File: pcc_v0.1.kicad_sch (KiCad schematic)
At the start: 54 parts, among them J1 Conn_01x04_Socket, J2 Conn_01x04_Socket, J4 Conn_02x14_Counter_Clockwise, J6 Conn_01x04_Socket, J7 Conn_01x04_Socket, J8 Conn_01x04_Socket, K2 CPC1706, K3 G7L-2A-X-L_DC12, Q2 BS108, U2 4N35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

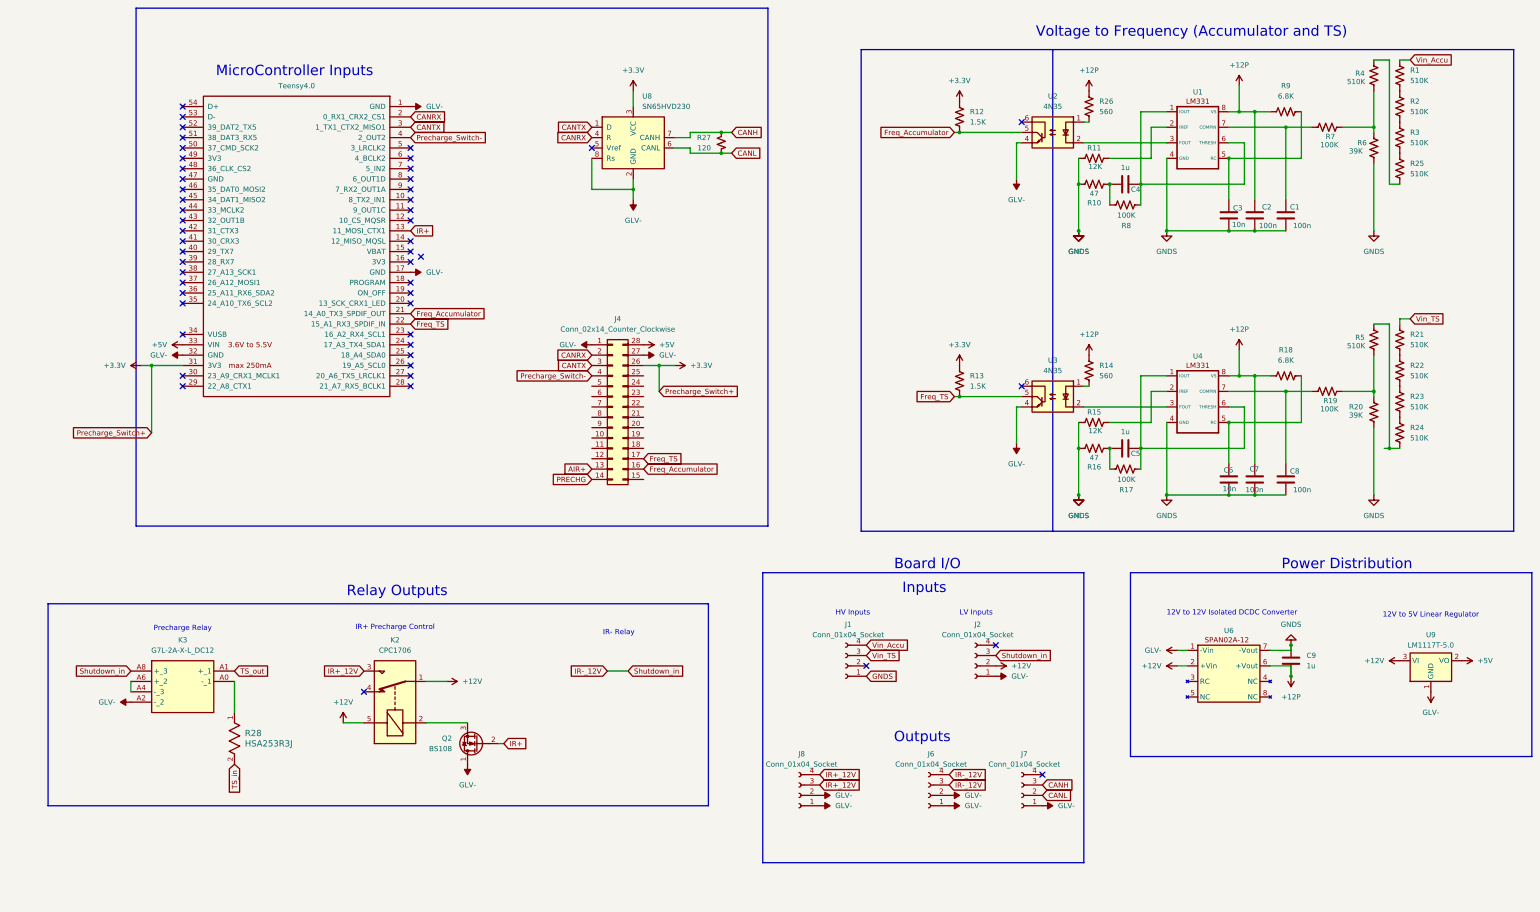
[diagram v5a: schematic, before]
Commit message: looking to add discharge relay
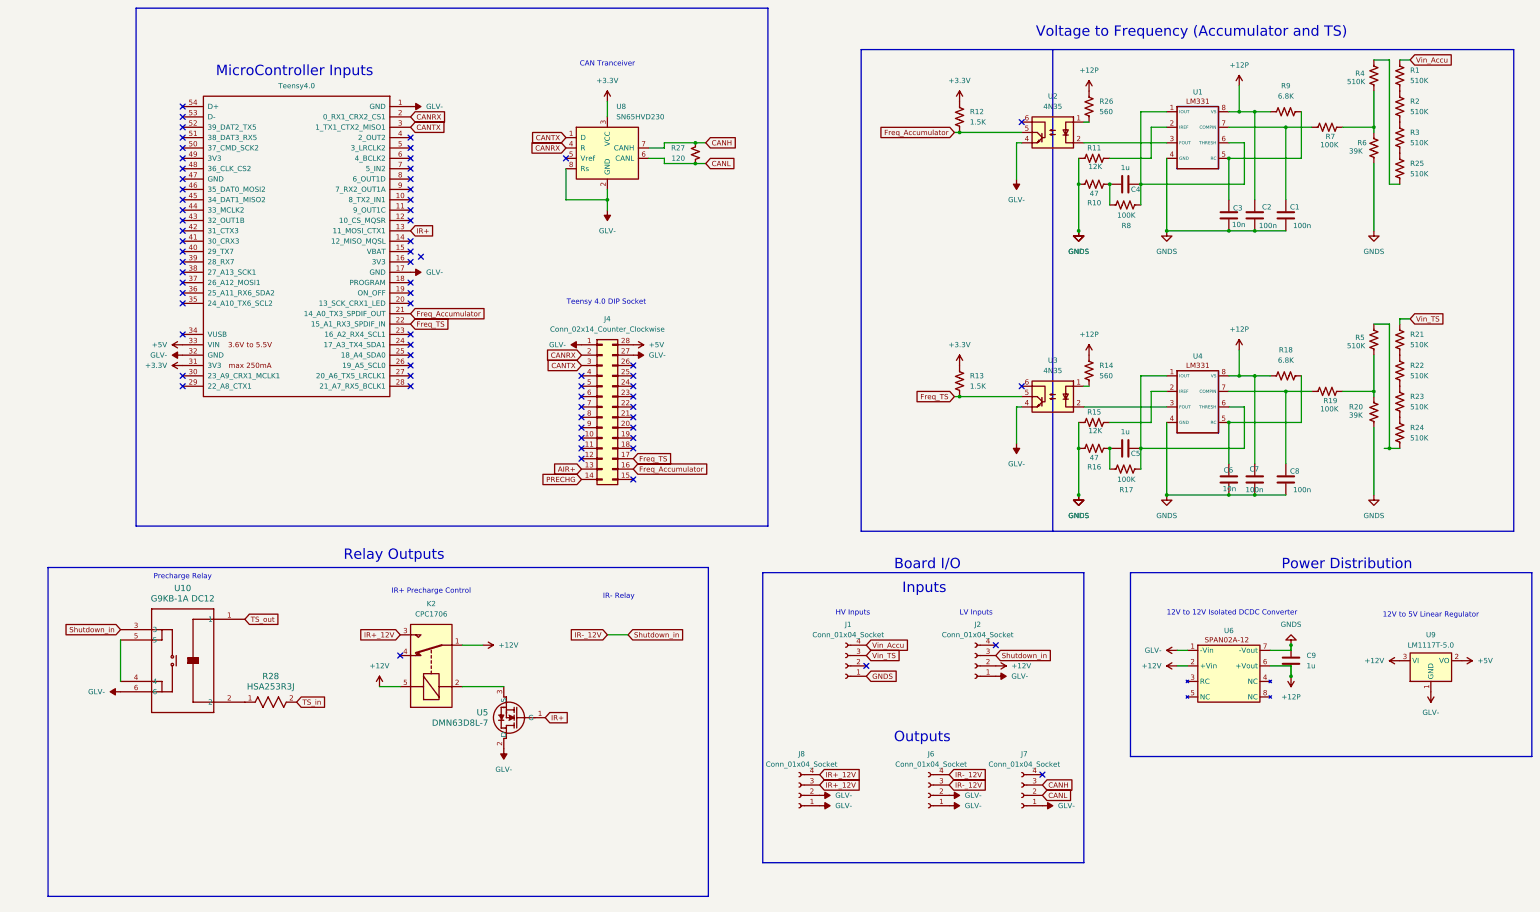
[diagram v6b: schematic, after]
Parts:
- removed K3: G7L-2A-X-L_DC12, KiCad:G7L2AXLDC12, symbol G7L-2A-X-L_DC12:G7L-2A-X-L_DC12
- removed Q2: BS108, Package_TO_SOT_THT:TO-92_Inline, symbol Transistor_FET:BS108
- added U10: G9KB-1A DC12, RELAY_G9KB-1A_OMR, symbol 2025-01-28_22-57-52:G9KB-1A_DC12
- added U5: DMN63D8L-7, nmos:SOIC_63D8L-7_DIO, symbol 2025-01-28_19-23-41:DMN63D8L-7
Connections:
- net +3.3V: no longer J4.26 (Pin_26)
- net GLV-: now also U10.6, U5.2 (D)
- net IR+: now also U5.1 (G)
- net IR-_12V: now also U10.3
- net TS_out: now also U10.1
- net at R28.1: now also U10.2
- net at K2.2: now also U5.3 (S)
- net Precharge_Switch-: no longer names the net of U7.4 (2_OUT2)
- net Precharge_Switch-: no longer J4.4 (Pin_4)
- new net: U10.4, U10.5
- no-connect marks 51 -> 71
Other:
- note added: "CAN Tranceiver"
- note added: "Teensy 4.0 DIP Socket"
- moved on the sheet: J4, K2, R27, R28, U8

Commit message: routed pcb
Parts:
- removed U10: G9KB-1A DC12, RELAY_G9KB-1A_OMR, symbol 2025-01-28_22-57-52:G9KB-1A_DC12
- added J3: Conn_01x04_Socket, Connector_Molex:Molex_Mini-Fit_Jr_5566-04A2_2x02_P4.20mm_Vertical, symbol Connector:Conn_01x04_Socket
- added J5: Conn_01x06_Socket, Connector_Molex:Molex_Mini-Fit_Jr_5566-06A2_2x03_P4.20mm_Vertical, symbol Connector:Conn_01x06_Socket
- added K1: G9KB-1A_DC12, precharge relay 2:G9KB1ADC12, symbol G9KB-1A_DC12:G9KB-1A_DC12
- R28: footprint footprints:RES_HSA25_TYCO_TYC -> precharge res:RES_HSA25_TYCO_TYC
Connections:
- net AIR+ is gone; now on net IR+: J4.13 (Pin_13)
- net TS_in is gone; now on net Vin_Accu: R28.2
- net +3.3V: now also J4.26 (Pin_26)
- net CANH: now also J7.4 (Pin_4); no longer J7.3 (Pin_3)
- net CANL: now also J7.3 (Pin_3); no longer J7.2 (Pin_2)
- net GLV-: now also J3.1 (Pin_1), J3.2 (Pin_2), K1.2 (COIL_2)
- net GNDS: now also J5.1 (Pin_1); no longer J1.1 (Pin_1)
- net Vin_Accu: now also K1.B4; no longer J1.4 (Pin_4)
- net DISCHRG_COM: now reaches J1.2 (Pin_2)
- net DISCHRG_COM: now also J1.1 (Pin_1), J5.4 (Pin_4)
- net B+_out: now reaches R28.1
- net B+_out: now also R21.1, J5.2 (Pin_2)
- net IR-_12V renamed DISCHRG_COIL+
- net DISCHRG_COIL+: now also J3.3 (Pin_3), J3.4 (Pin_4), K1.1 (COIL_1)
- net PRECHG: no longer names the net of J4.14 (Pin_14)
- net Vin_TS renamed DISCHRG_NO
- net DISCHRG_NO: now also J1.4 (Pin_4), J5.5 (Pin_5); no longer R21.1
- new net: K1.A4, K1.B3
- new net B+_in: J5.3 (Pin_3), K1.A3
- no-connect marks 71 -> 70
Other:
- moved on the sheet: J6, J7, J8, R28

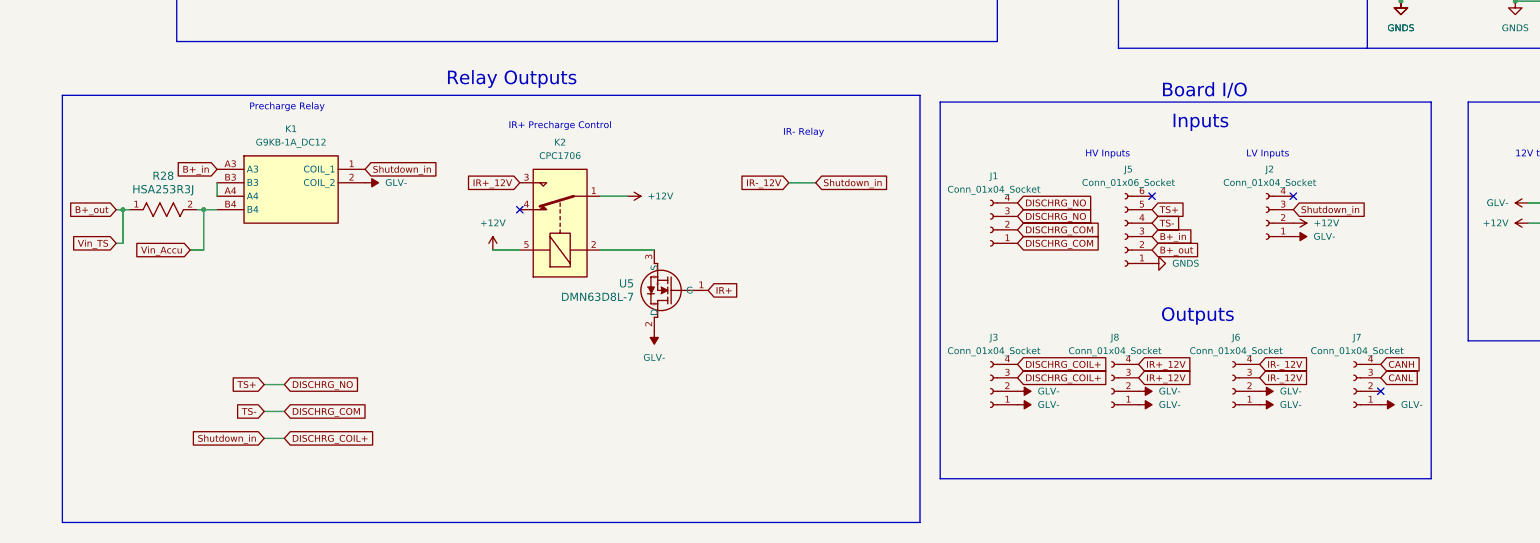
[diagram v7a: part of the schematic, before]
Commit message: next round of changes with correct precharge resistor and isolation distance
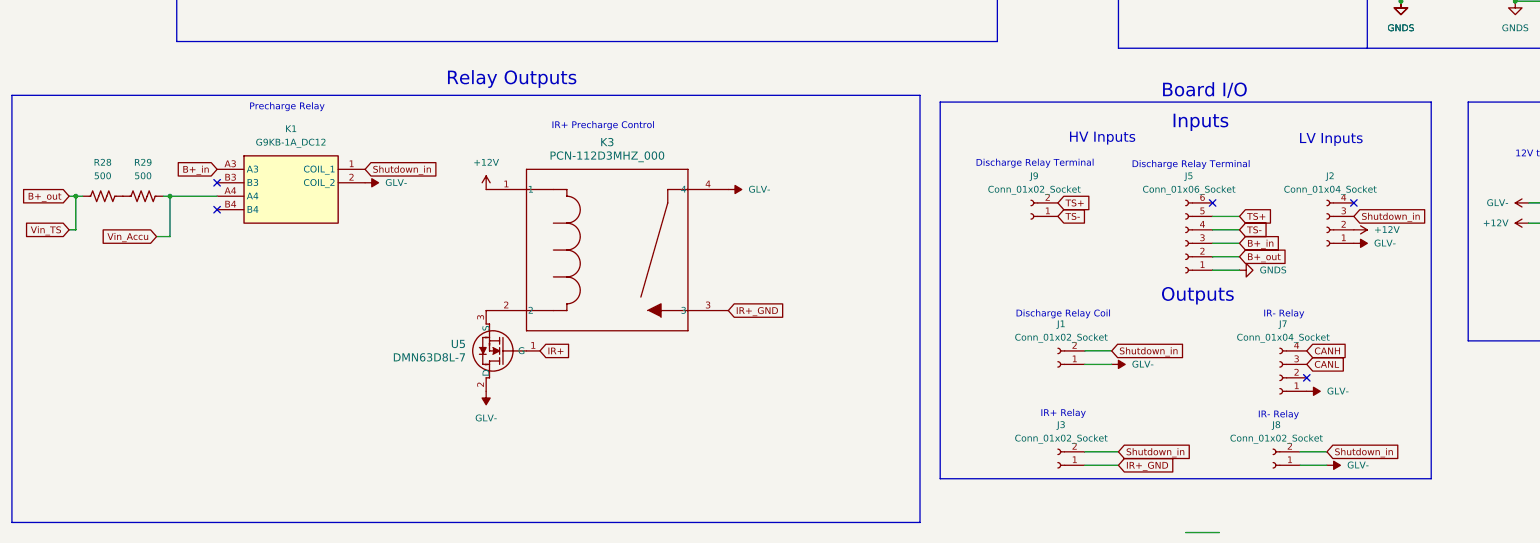
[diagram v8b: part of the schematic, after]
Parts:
- removed J1, J3, J6, J8: Conn_01x04_Socket, Connector_Molex:Molex_Mini-Fit_Jr_5566-04A2_2x02_P4.20mm_Vertical, symbol Connector:Conn_01x04_Socket
- removed K2: CPC1706, Relay_THT:Relay_SPDT_SANYOU_SRD_Series_Form_C, symbol Relay:SANYOU_SRD_Form_C
- removed R28: HSA253R3J, precharge res:RES_HSA25_TYCO_TYC, symbol 2025-01-28_17-59-30:HSA253R3J
- added J1, J3, J8, J9: Conn_01x02_Socket, Connector_Molex:Molex_Mini-Fit_Jr_5566-02A2_2x01_P4.20mm_Vertical, symbol Connector:Conn_01x02_Socket
- added K3: PCN-112D3MHZ_000, PCN_112D3HMZ:RELAY_PCN-105D3MHZ_000_TEC, symbol PCN_112D3HMZ:PCN-112D3MHZ_000
- added R28, R29: 500, precharge res:Ohmite HS100 500R F, symbol Device:R_US
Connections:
- net +12V: now also K3.1
- net B+_out: now also R28.1
- net GLV-: now also J1.1 (Pin_1), J8.1 (Pin_1), K3.4
- net Vin_Accu: now also K1.A4, R29.2; no longer K1.B4
- net at K1.B3: no longer K1.A4
- net at U5.3 (S): now also K3.2
- net DISCHRG_COIL+ renamed Shutdown_in
- net Shutdown_in: now also J1.2 (Pin_2), J3.2 (Pin_2), J8.2 (Pin_2)
- net DISCHRG_COM renamed TS-
- net TS-: now also J9.1 (Pin_1)
- net DISCHRG_NO renamed TS+
- net TS+: now also J9.2 (Pin_2)
- new net: R28.2, R29.1
- new net IR+_GND: J3.1 (Pin_1), K3.3
- no-connect marks 70 -> 71
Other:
- note added: "Discharge Relay Coil"
- note added: "Discharge Relay Terminal"
- note added: "IR+ Relay"
- moved on the sheet: J2, J5, J7, U5
